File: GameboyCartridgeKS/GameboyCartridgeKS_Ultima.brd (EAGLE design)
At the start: 49.3 x 58 mm, 29 parts, among them IC1 AT49F040J

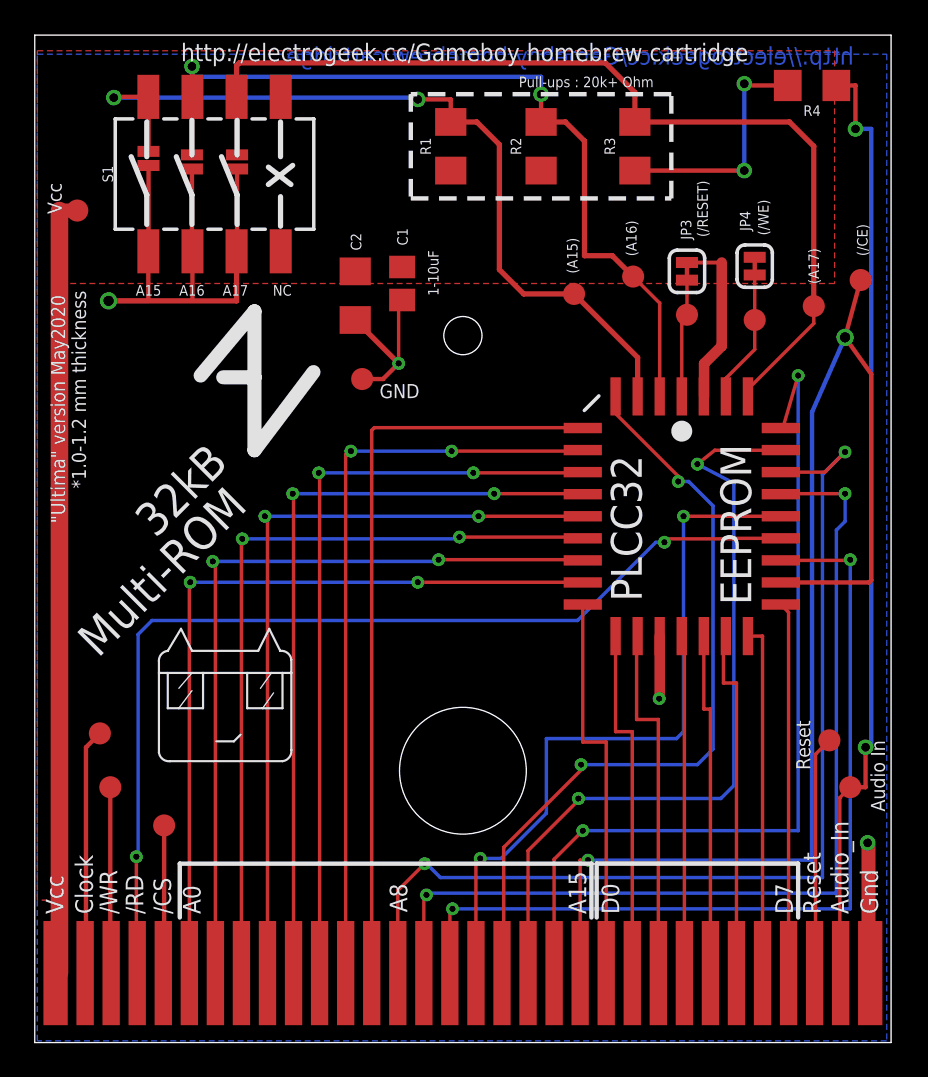
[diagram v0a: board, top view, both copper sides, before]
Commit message: Added solderpad for the RD signal, and the post-migration missing gitignore file
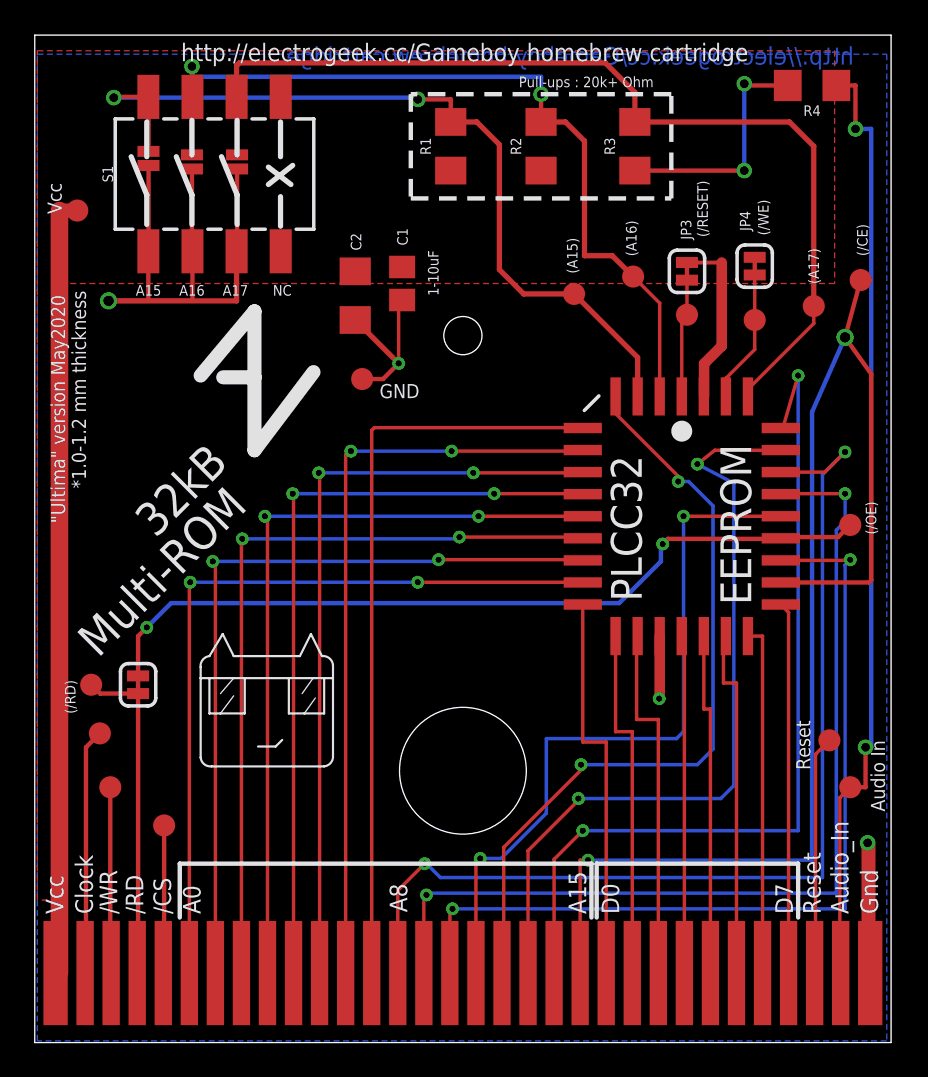
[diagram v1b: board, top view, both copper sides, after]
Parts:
- added JP6: JUMPER-SMT_2_NC_TRACE_SILK, SparkFun-Jumpers:SMT-JUMPER_2_NC_TRACE_SILK
- added TP14, TP15: TEST-POINT3X5, SparkFun-Connectors:PAD.03X.05
- moved U$3 2.42 mm to (10.4, 15.9)
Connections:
- new net N$3: IC1.24, JP6.2, TP15.P$1
- net 4: now also JP6.1, TP14.P$1; no longer IC1.24
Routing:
- net N$3: track 0.00 -> 46.5 mm, vias 0 -> 2
- net 4: track 58.9 -> 19.0 mm, vias 2 -> 0
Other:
- board text added: "(/OE)"
- board text added: "(/RD)"
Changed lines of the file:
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@@
 <wire x1="37.5" y1="54.6" x2="22.5" y2="54.6" width="0.254" layer="21" style="shortdash"/>
 <text x="32.6" y="55" size="0.6096" layer="21" font="vector" ratio="20" align="bottom-center">Pull-ups : 20k+ Ohm</text>
+<text x="3.2" y="19.9" size="0.6096" layer="21" font="vector" ratio="20" rot="R90" align="bottom-center">(/RD)</text>
+<text x="49.3" y="30.2" size="0.6096" layer="21" font="vector" ratio="20" rot="R90" align="bottom-center">(/OE)</text>
 </plain>
 <attributes>
@@
 <element name="TP8" library="SparkFun-Connectors" library_urn="urn:adsk.eagle:library:513" package="PAD.03X.05" package3d_urn="urn:adsk.eagle:package:38285/1" value="TEST-POINT3X5" x="46.6" y="17.4" smashed="yes"/>
 <element name="U$2" library="kalshagar-images" package="GAMEBOY_LOGO" value="" x="21.2" y="21" smashed="yes"/>
-<element name="U$3" library="kalshagar-images" package="PIGMAN1" value="" x="8" y="16.2" smashed="yes"/>
+<element name="U$3" library="kalshagar-images" package="PIGMAN1" value="" x="10.4" y="15.9" smashed="yes"/>
 <element name="TP9" library="SparkFun-Connectors" library_urn="urn:adsk.eagle:library:513" package="PAD.03X.05" package3d_urn="urn:adsk.eagle:package:38285/1" value="TEST-POINT3X5" x="5.2" y="14.7" smashed="yes"/>
 <element name="TP10" library="SparkFun-Connectors" library_urn="urn:adsk.eagle:library:513" package="PAD.03X.05" package3d_urn="urn:adsk.eagle:package:38285/1" value="TEST-POINT3X5" x="8.3" y="12.5" smashed="yes"/>
@@
 <attribute name="VALUE" x="11.357" y="50.7" size="0.6096" layer="27" font="vector" ratio="20" rot="R270" align="top-center"/>
 </element>
+<element name="TP14" library="SparkFun-Connectors" library_urn="urn:adsk.eagle:library:513" package="PAD.03X.05" package3d_urn="urn:adsk.eagle:package:38285/1" value="TEST-POINT3X5" x="4.1" y="20.6" smashed="yes"/>
+<element name="JP6" library="SparkFun-Jumpers" package="SMT-JUMPER_2_NC_TRACE_SILK" package3d_urn="urn:adsk.eagle:package:39281/1" value="JUMPER-SMT_2_NC_TRACE_SILK" x="6.8" y="20.6" smashed="yes" rot="R90">
+<attribute name="VALUE" x="7.943" y="20.6" size="0.6096" layer="27" font="vector" ratio="20" rot="R90" align="top-center"/>
+</element>
+<element name="TP15" library="SparkFun-Connectors" library_urn="urn:adsk.eagle:library:513" package="PAD.03X.05" package3d_urn="urn:adsk.eagle:package:38285/1" value="TEST-POINT3X5" x="47.8" y="29.8" smashed="yes"/>
 </elements>
 <signals>
@@
 <signal name="4">
 <contactref element="U$1" pad="4"/>
-<contactref element="IC1" pad="24"/>
-<wire x1="43.8" y1="29.03" x2="41.13" y2="29.03" width="0.2" layer="1"/>
-<wire x1="41.13" y1="29.03" x2="41.1" y2="29" width="0.2" layer="1"/>
-<wire x1="41.1" y1="29" x2="37.3" y2="29" width="0.2" layer="1"/>
-<wire x1="37.1" y1="28.8" x2="37.3" y2="29" width="0.2" layer="1"/>
-<via x="37.1" y="28.8" extent="1-16" drill="0.35"/>
-<wire x1="37.1" y1="28.8" x2="36.6" y2="28.8" width="0.2" layer="16"/>
-<wire x1="36.6" y1="28.8" x2="32.1" y2="24.3" width="0.2" layer="16"/>
-<wire x1="32.1" y1="24.3" x2="7.6" y2="24.3" width="0.2" layer="16"/>
-<wire x1="7.6" y1="24.3" x2="6.8" y2="23.5" width="0.2" layer="16"/>
-<wire x1="6.7" y1="10.7" x2="6.8" y2="10.8" width="0.2" layer="16"/>
-<wire x1="6.8" y1="23.5" x2="6.8" y2="10.8" width="0.2" layer="16"/>
-<via x="6.7" y="10.7" extent="1-16" drill="0.35"/>
-<wire x1="6.7" y1="10.7" x2="6.7" y2="4.05" width="0.2" layer="1"/>
-<wire x1="6.7" y1="4.05" x2="6.75" y2="4" width="0.2" layer="1"/>
+<wire x1="6.8" y1="4.05" x2="6.75" y2="4" width="0.2" layer="1"/>
+<contactref element="TP14" pad="P$1"/>
+<contactref element="JP6" pad="1"/>
+<wire x1="6.8" y1="20.092" x2="6.8" y2="4.05" width="0.254" layer="1"/>
+<wire x1="6.8" y1="20.092" x2="4.608" y2="20.092" width="0.254" layer="1"/>
+<wire x1="4.608" y1="20.092" x2="4.1" y2="20.6" width="0.254" layer="1"/>
 </signal>
 <signal name="11">
@@
 <wire x1="24.75" y1="7.55" x2="24.9" y2="7.7" width="0.2" layer="1"/>
 <via x="24.9" y="7.7" extent="1-16" drill="0.35"/>
-<wire x1="24.9" y1="7.7" x2="47.8" y2="7.7" width="0.2" layer="16"/>
-<wire x1="47.8" y1="7.7" x2="47.8" y2="27.8" width="0.2" layer="16"/>
+<wire x1="24.9" y1="7.7" x2="47.5" y2="7.7" width="0.2" layer="16"/>
+<wire x1="47.5" y1="27.5" x2="47.5" y2="7.7" width="0.2" layer="16"/>
+<wire x1="47.5" y1="27.5" x2="47.8" y2="27.8" width="0.2" layer="16"/>
 <via x="47.8" y="27.8" extent="1-16" drill="0.35"/>
 <wire x1="47.8" y1="27.8" x2="47.76" y2="27.76" width="0.2" layer="1"/>
@@
 <wire x1="12.5" y1="54.445" x2="12.47" y2="54.445" width="0.254" layer="1"/>
 </signal>
+<signal name="N$3">
+<contactref element="IC1" pad="24"/>
+<contactref element="JP6" pad="2"/>
+<wire x1="6.8" y1="21.108" x2="6.8" y2="23.4" width="0.254" layer="1"/>
+<wire x1="6.8" y1="23.4" x2="7.3" y2="23.9" width="0.254" layer="1"/>
+<via x="7.3" y="23.9" extent="1-16" drill="0.35"/>
+<wire x1="7.3" y1="23.9" x2="8.7" y2="25.3" width="0.254" layer="16"/>
+<wire x1="8.7" y1="25.3" x2="34.5" y2="25.3" width="0.254" layer="16"/>
+<wire x1="34.5" y1="25.3" x2="36.9" y2="27.7" width="0.254" layer="16"/>
+<wire x1="36.9" y1="27.7" x2="36.9" y2="28.7" width="0.254" layer="16"/>
+<wire x1="36.9" y1="28.7" x2="37" y2="28.7" width="0.254" layer="16"/>
+<via x="37" y="28.7" extent="1-16" drill="0.35"/>
+<wire x1="37" y1="28.7" x2="37.3" y2="29" width="0.254" layer="1"/>
+<wire x1="43.77" y1="29" x2="37.3" y2="29" width="0.254" layer="1"/>
+<wire x1="43.77" y1="29" x2="43.8" y2="29.03" width="0.254" layer="1"/>
+<contactref element="TP15" pad="P$1"/>
+<wire x1="43.8" y1="29.03" x2="43.87" y2="29.1" width="0.254" layer="1"/>
+<wire x1="43.87" y1="29.1" x2="47.1" y2="29.1" width="0.254" layer="1"/>
+<wire x1="47.1" y1="29.1" x2="47.8" y2="29.8" width="0.254" layer="1"/>
+</signal>
 </signals>

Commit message: Moved the PLCC a bit to the center
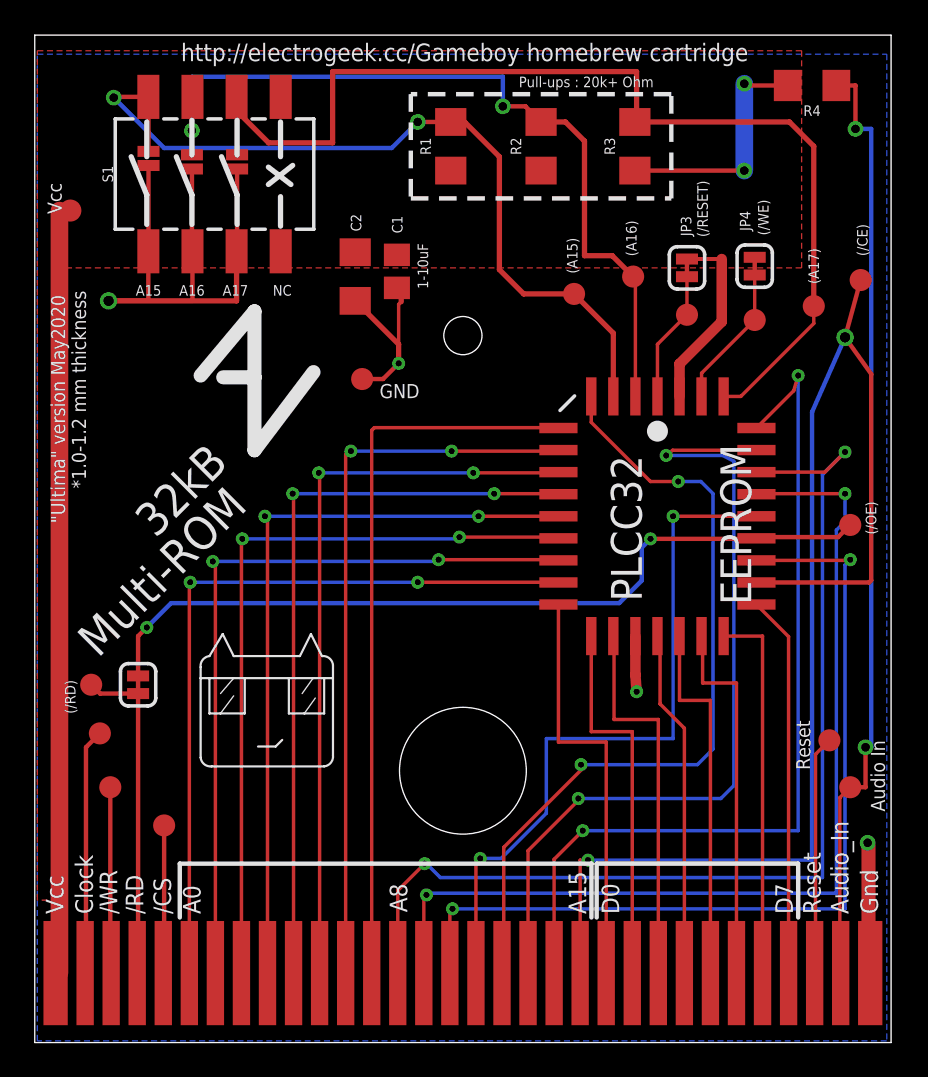
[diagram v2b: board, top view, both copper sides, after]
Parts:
- moved IC1 1.40 mm to (36.7, 30.3)
- moved C2 1.10 mm to (19.3, 44.1)
- moved C1 0.76 mm to (21.7, 44.4)
- moved TP6 0.40 mm to (2.90, 47.9)
- moved JP3 0.20 mm to (38.4, 44.6)
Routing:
- net N$9: track 57.5 -> 63.1 mm
- net 19: track 45.4 -> 48.5 mm
- net 18: track 44.9 -> 46.8 mm
- net N$8: track 49.0 -> 50.5 mm
- net GND: track 59.7 -> 61.2 mm
- net 8: track 44.8 -> 43.4 mm
- net 12: track 43.6 -> 42.2 mm
- net 9: track 44.7 -> 43.3 mm
- net 7: track 45.1 -> 43.7 mm
- net 28: track 20.3 -> 21.7 mm
- net 26: track 19.8 -> 21.2 mm
- net 23: track 20.4 -> 21.8 mm
- net 22: track 22.6 -> 24.0 mm
- net 16: track 50.6 -> 52.0 mm
- net 14: track 59.4 -> 60.8 mm
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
